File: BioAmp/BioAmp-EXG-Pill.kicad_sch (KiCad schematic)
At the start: 22 parts, among them IC1 MCP3221A4T-E_OT, J1 Conn_01x03_Pin, J2 Conn_01x04_Pin, J3 Conn_01x04_Pin, U1 Amp, U2 LOGO_UDLABS

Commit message: Changed bpf gain comment to x180 and added a .gitignore.
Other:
- note added: "180x Gain Bandpass Filter"
- note removed: "1000x Gain Bandpass Filter"

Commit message: Changed DRL R11 resistor to 1MegaOhm after improvement in signal quality after soldering one on.
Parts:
- R11: value 0R -> 1M
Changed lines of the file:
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@@
 			)
 		)
-		(property "Value" "0R"
+		(property "Value" "1M"
 			(at 109.474 162.052 90)
 			(show_name no)

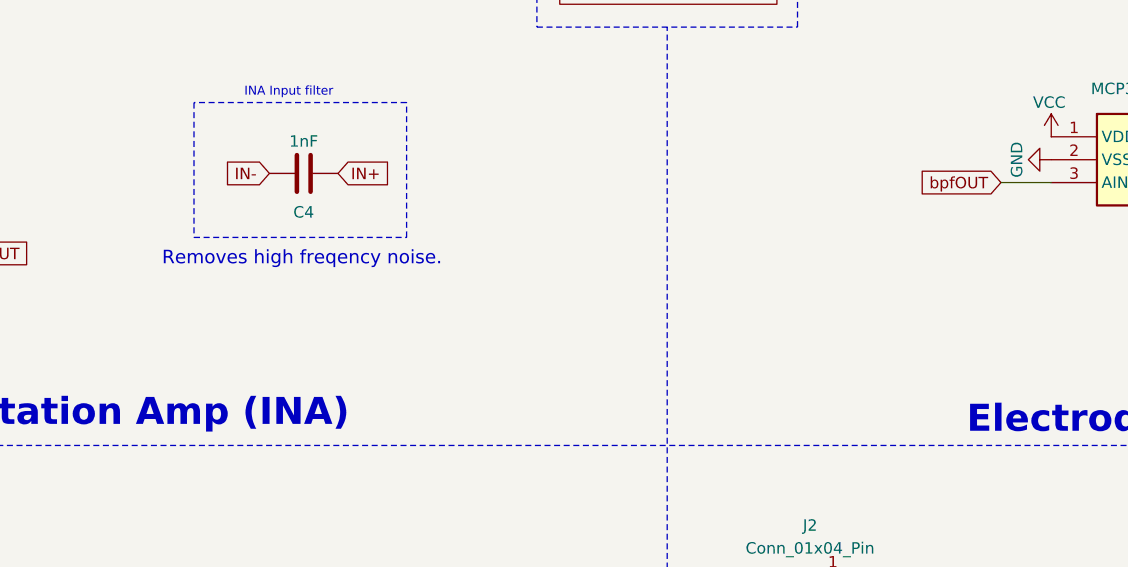
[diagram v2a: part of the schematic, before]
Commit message: Added Do Not Place marking on C4.
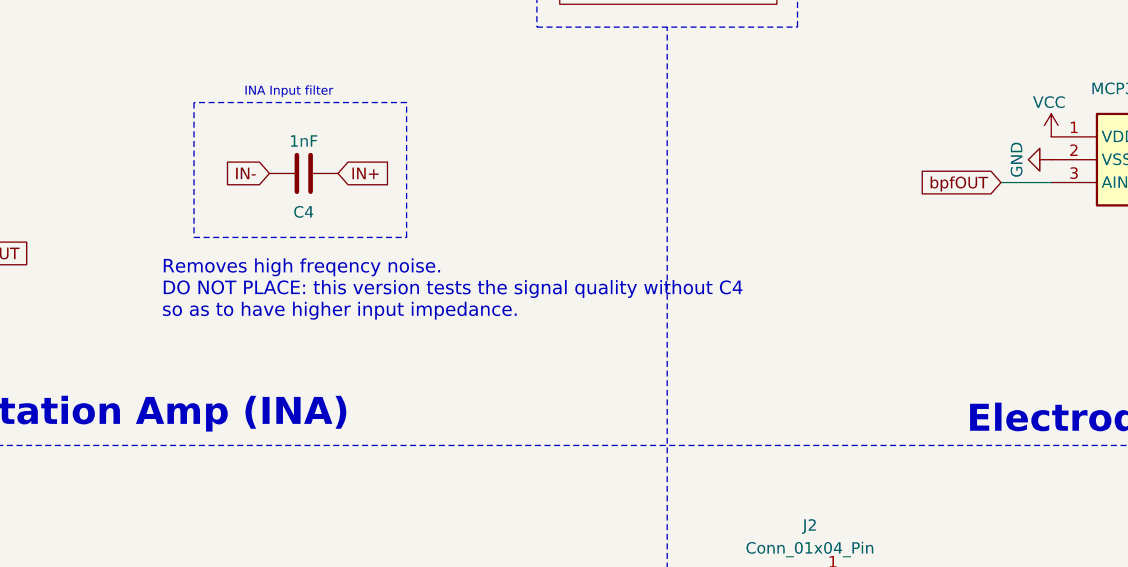
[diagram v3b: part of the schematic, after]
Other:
- note added: "Removes high freqency noise. DO NOT PLACE: this version tests the signal quality without C4 so as to have higher input impedance."
- note removed: "Removes high freqency noise."
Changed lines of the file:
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@@
 		)
 	)
-	(text "Removes high freqency noise."
+	(text "Removes high freqency noise. \nDO NOT PLACE: this version tests the signal quality without C4 \nso as to have higher input impedance."
 		(exclude_from_sim no)
-		(at 120.904 51.562 0)
+		(at 120.904 57.404 0)
 		(effects
 			(font

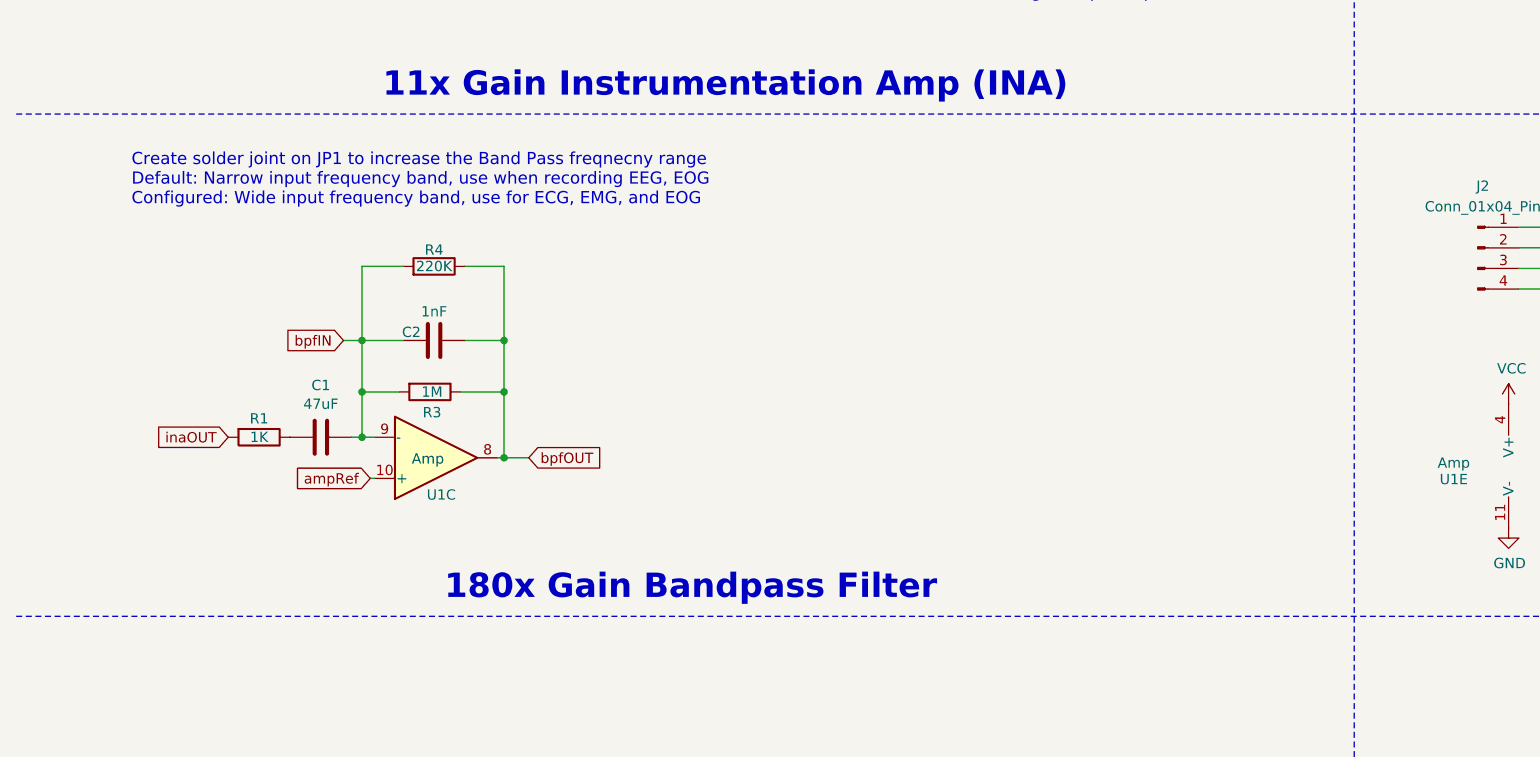
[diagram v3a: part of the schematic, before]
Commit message: Changed bandpass gain to x73 and cutoff frequencies to 20 Hz and 500 Hz.
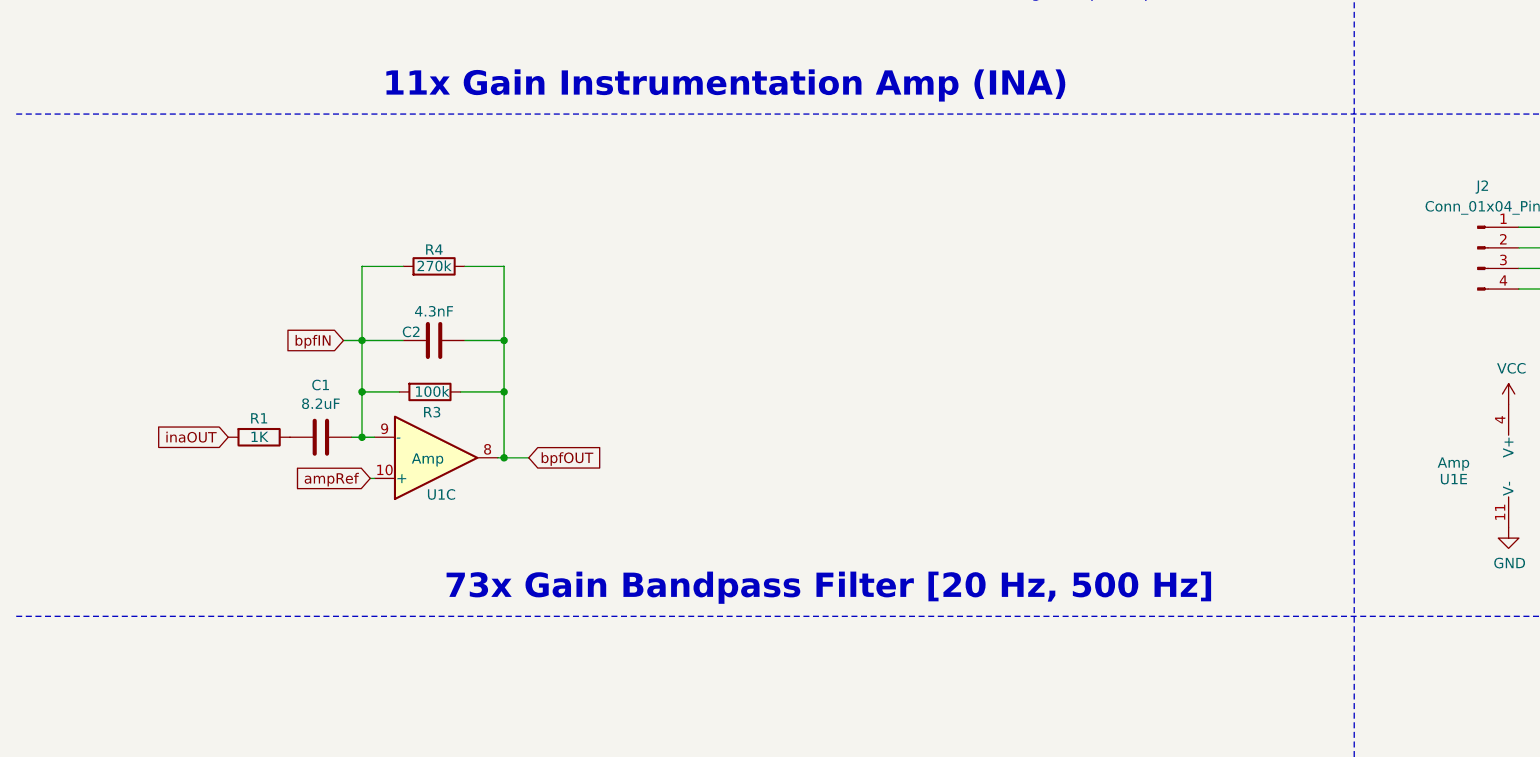
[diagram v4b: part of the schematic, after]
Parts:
- C1: value 47uF -> 8.2uF
- C2: value 1nF -> 4.3nF
- R3: value 1M -> 100k
- R4: value 220K -> 270k
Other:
- note added: "73x Gain Bandpass Filter [20 Hz, 500 Hz]"
- note removed: "180x Gain Bandpass Filter"
- note removed: "Create solder joint on JP1 to increase the Band Pass freqnecny range Default: Narrow input frequency band, use when recording EEG, EOG Configured: Wide input frequency band, use for ECG, EMG, and EOG"
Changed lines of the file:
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@@
 		)
 	)
-	(text "180x Gain Bandpass Filter"
+	(text "73x Gain Bandpass Filter [20 Hz, 500 Hz]"
 		(exclude_from_sim no)
 		(at 64.77 131.572 0)
@@
 		)
 	)
-	(text "Create solder joint on JP1 to increase the Band Pass freqnecny range\nDefault: Narrow input frequency band, use when recording EEG, EOG\nConfigured: Wide input frequency band, use for ECG, EMG, and EOG"
-		(exclude_from_sim no)
-		(at 26.162 82.804 0)
-		(effects
-			(font
-				(size 1.4986 1.4986)
-			)
-			(justify left bottom)
-		)
-	)
 	(text "Header pins / Connectors"
 		(exclude_from_sim no)
@@
 			)
 		)
-		(property "Value" "1nF"
+		(property "Value" "4.3nF"
 			(at 63.5 95.758 90)
 			(show_name no)
@@
 			)
 		)
-		(property "Value" "1M"
+		(property "Value" "100k"
 			(at 63.246 105.664 90)
 			(show_name no)
@@
 			)
 		)
-		(property "Value" "47uF"
+		(property "Value" "8.2uF"
 			(at 49.53 107.1626 90)
 			(show_name no)
@@
 			)
 		)
-		(property "Value" "220K"
+		(property "Value" "270k"
 			(at 63.5 90.17 90)
 			(show_name no)

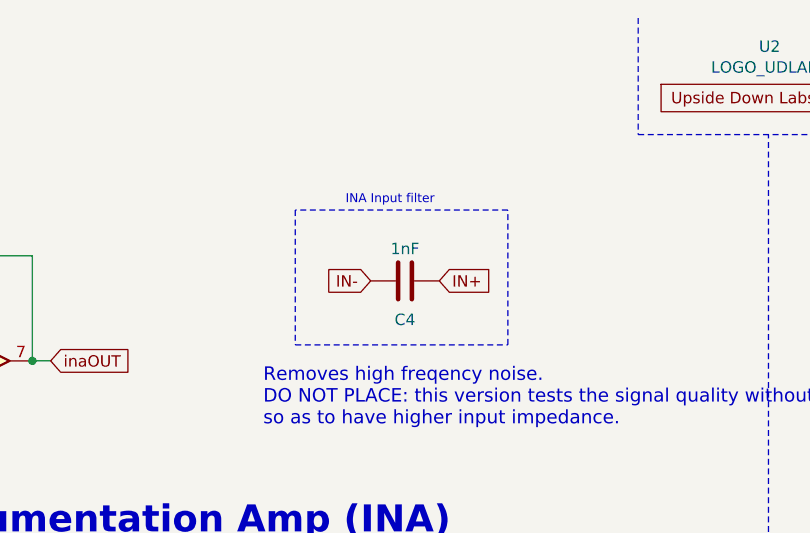
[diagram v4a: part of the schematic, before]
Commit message: Changed C4 to 10pF to increase impedance.
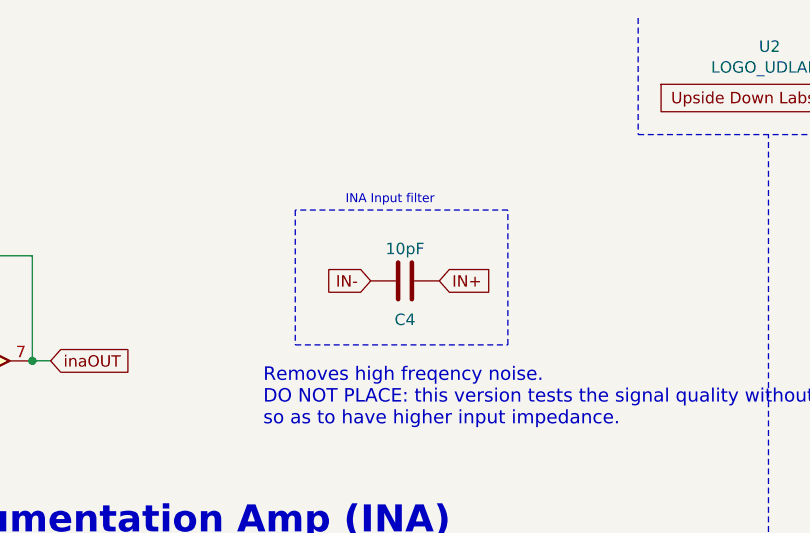
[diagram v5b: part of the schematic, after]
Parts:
- C4: value 1nF -> 10pF
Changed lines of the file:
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@@
 			)
 		)
-		(property "Value" "1nF"
+		(property "Value" "10pF"
 			(at 136.652 37.592 90)
 			(show_name no)

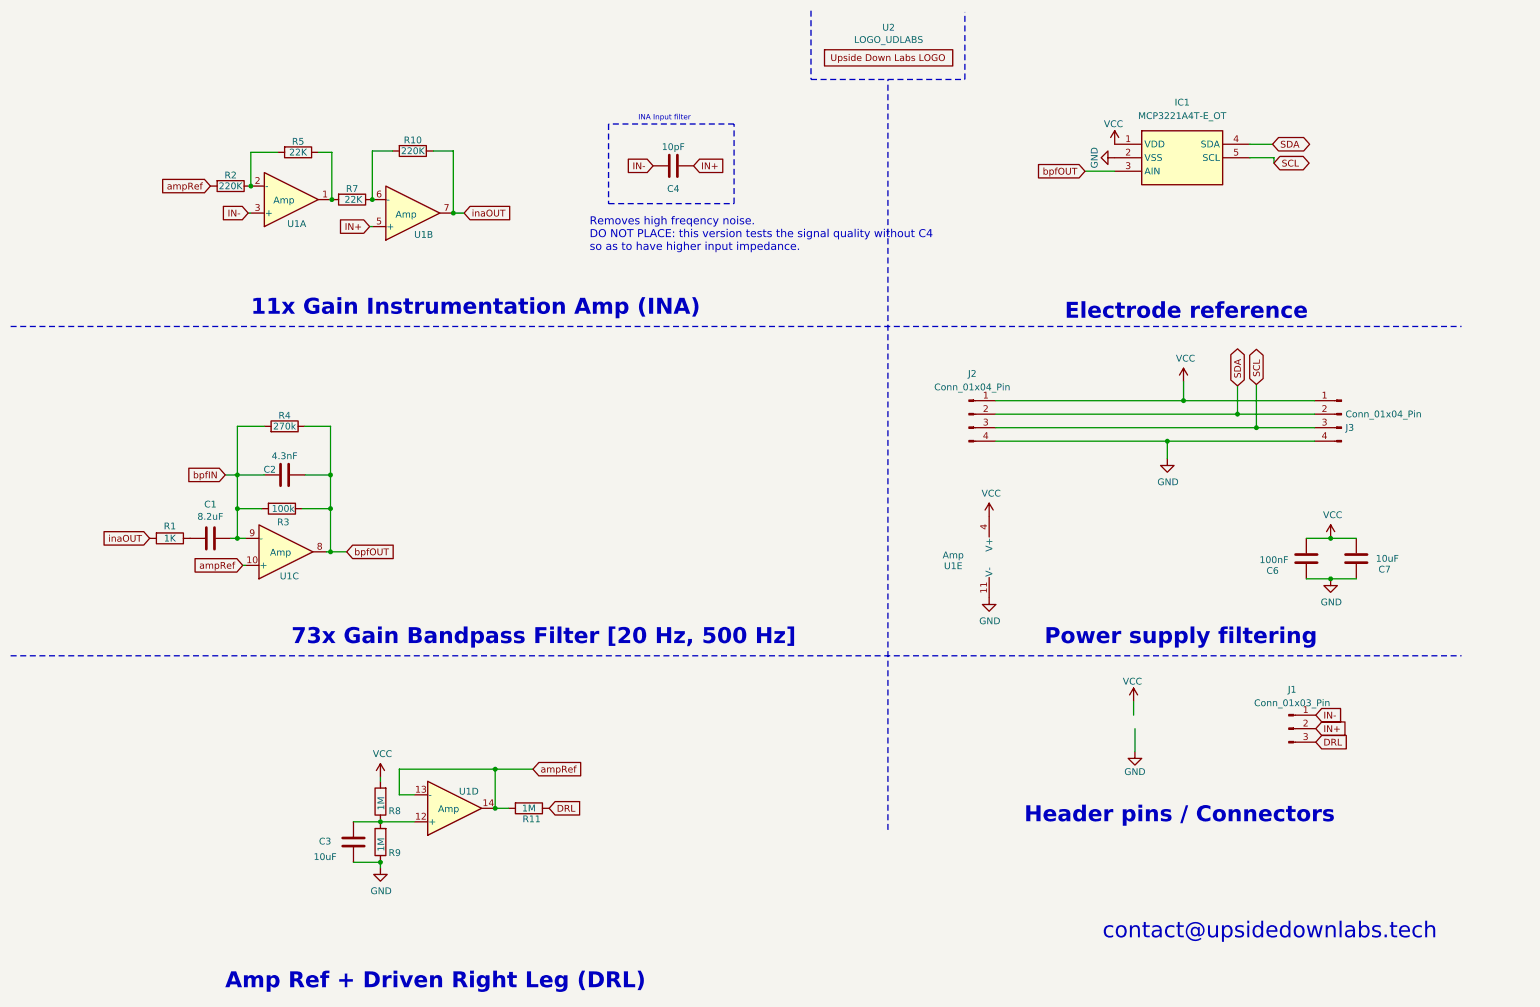
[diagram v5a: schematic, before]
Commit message: Added TVS diodes
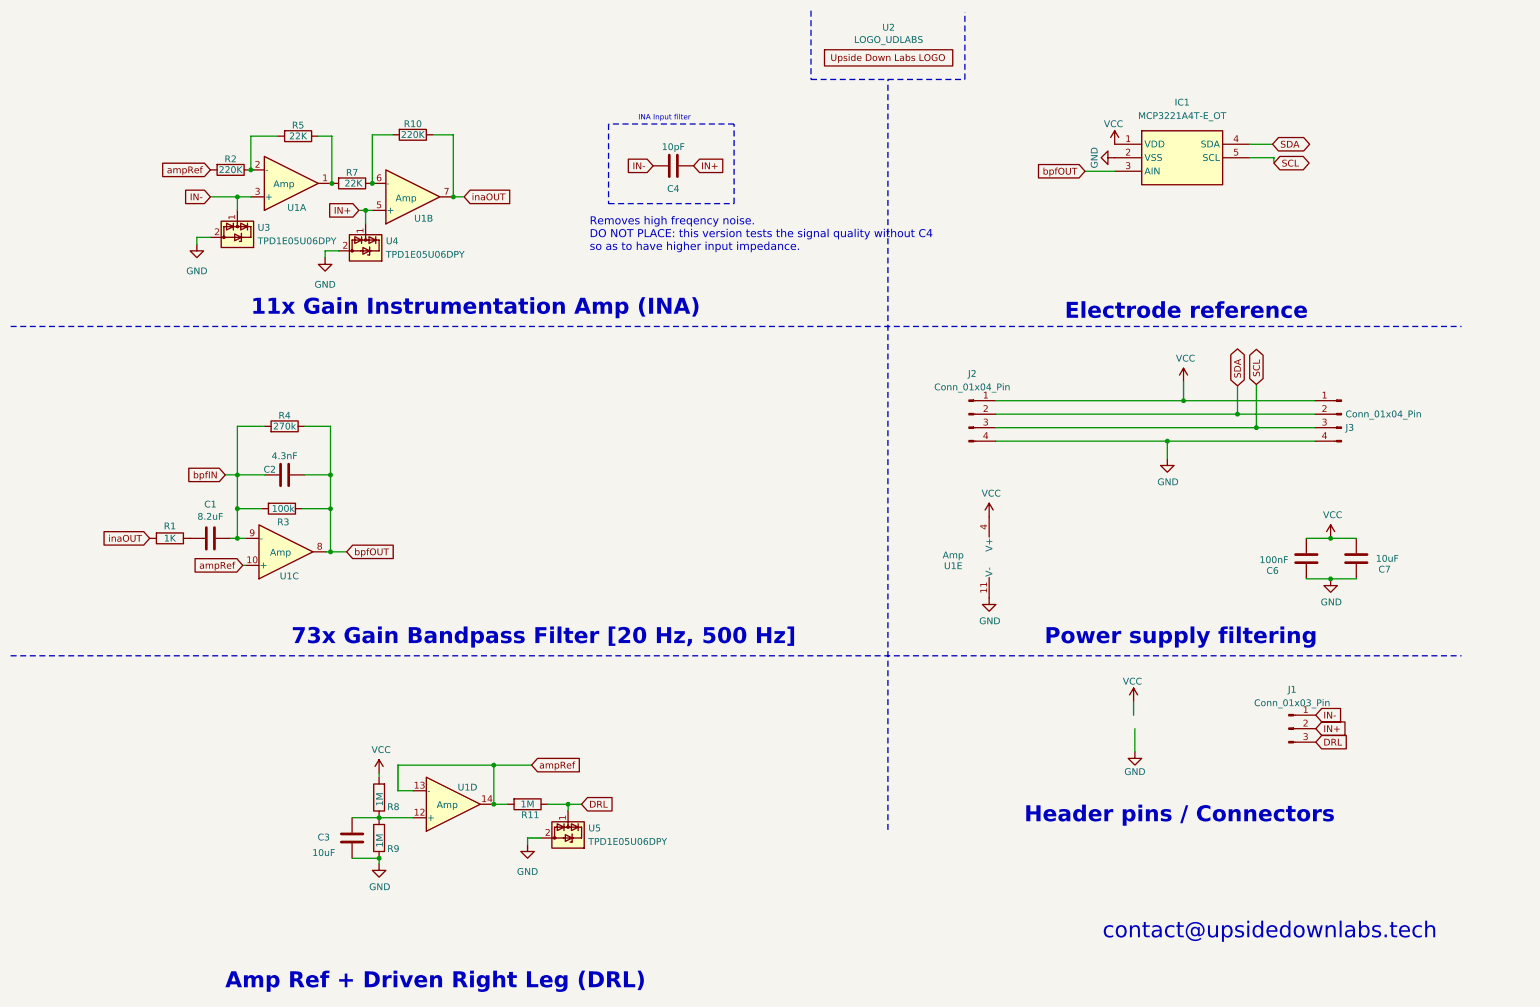
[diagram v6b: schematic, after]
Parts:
- added U3, U4, U5: TPD1E05U06DPY, Package_SON:Texas_DPY0002A_0.6x1mm_P0.65mm, symbol Power_Protection:TPD1E05U06DPY
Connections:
- net DRL: now also U5.1 (I/O)
- net GND: now also U3.2 (GND), U4.2 (GND), U5.2 (GND)
- net IN+: now also U4.1 (I/O)
- net IN-: now also U3.1 (I/O)
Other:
- moved on the sheet: C3, R10, R11, R2, R5, R7, R8, R9, U1B, U1D

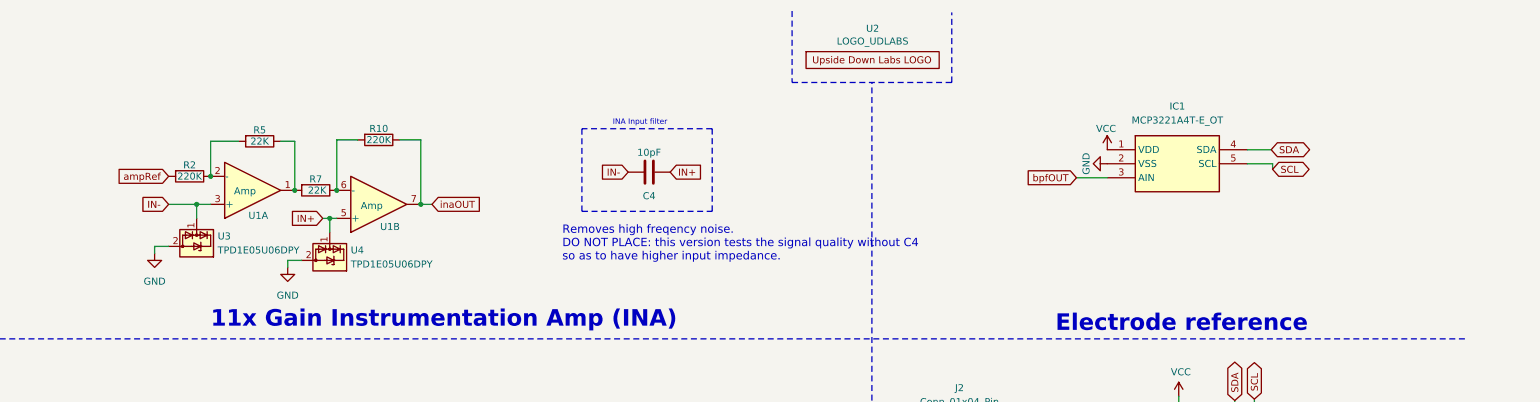
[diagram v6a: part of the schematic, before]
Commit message: Added series resistor after ESD protection at opamp input, 2.2kohm
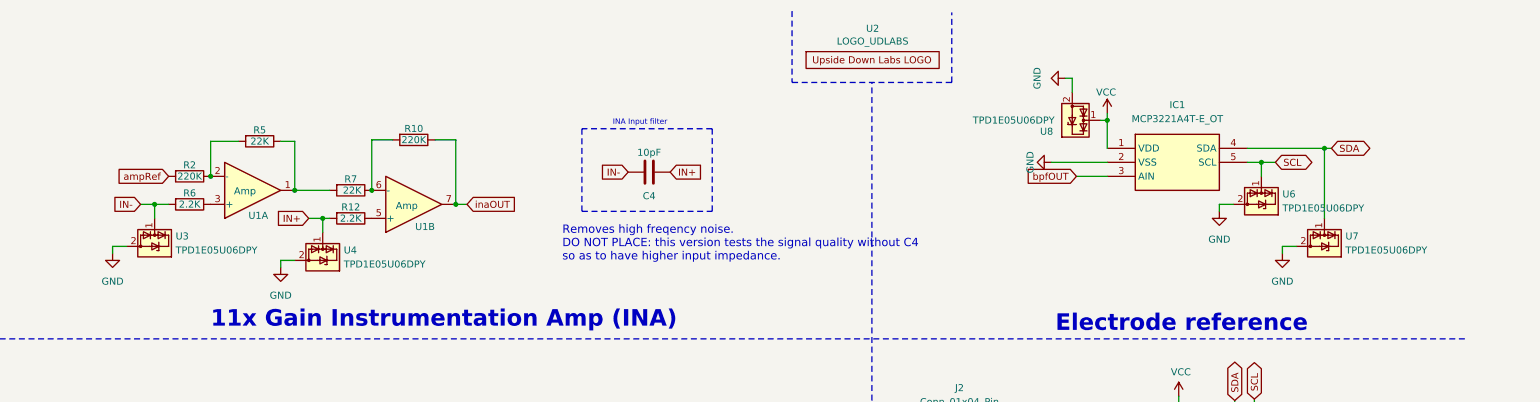
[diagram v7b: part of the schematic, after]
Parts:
- added R12, R6: 2.2K, Resistor_SMD:R_0603_1608Metric_Pad0.98x0.95mm_HandSolder, symbol Device:R
- added U6, U7, U8: TPD1E05U06DPY, Package_SON:Texas_DPY0002A_0.6x1mm_P0.65mm, symbol Power_Protection:TPD1E05U06DPY
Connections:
- net GND: now also U6.2 (GND), U7.2 (GND), U8.2 (GND)
- net IN+: now also R12.2; no longer U1.5 (+)
- net IN-: now also R6.2; no longer U1.3 (+)
- net SCL: now also U6.1 (I/O)
- net SDA: now also U7.1 (I/O)
- net VCC: now also U8.1 (I/O)
- new net: R12.1, U1.5 (+)
- new net: R6.1, U1.3 (+)
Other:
- moved on the sheet: R10, R7, U1B, U3, U4
